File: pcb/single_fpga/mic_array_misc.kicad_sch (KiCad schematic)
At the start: 44 parts

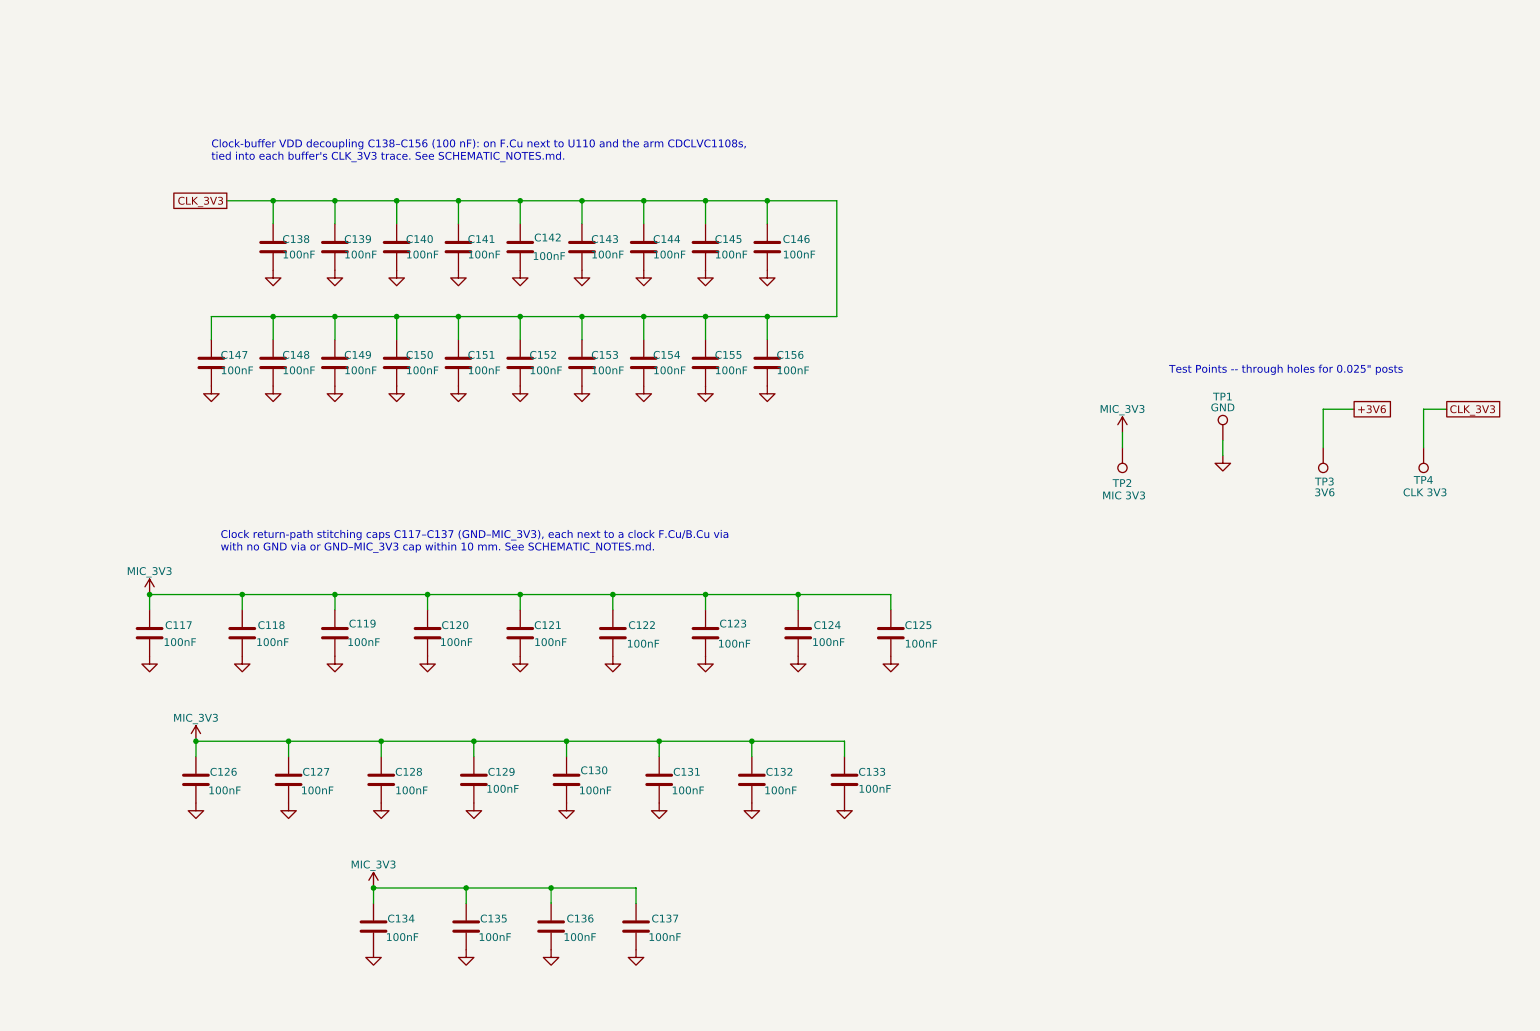
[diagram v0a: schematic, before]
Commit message: Added more stitching caps and vias. Carved +5V island in In2.Cu and renamed.
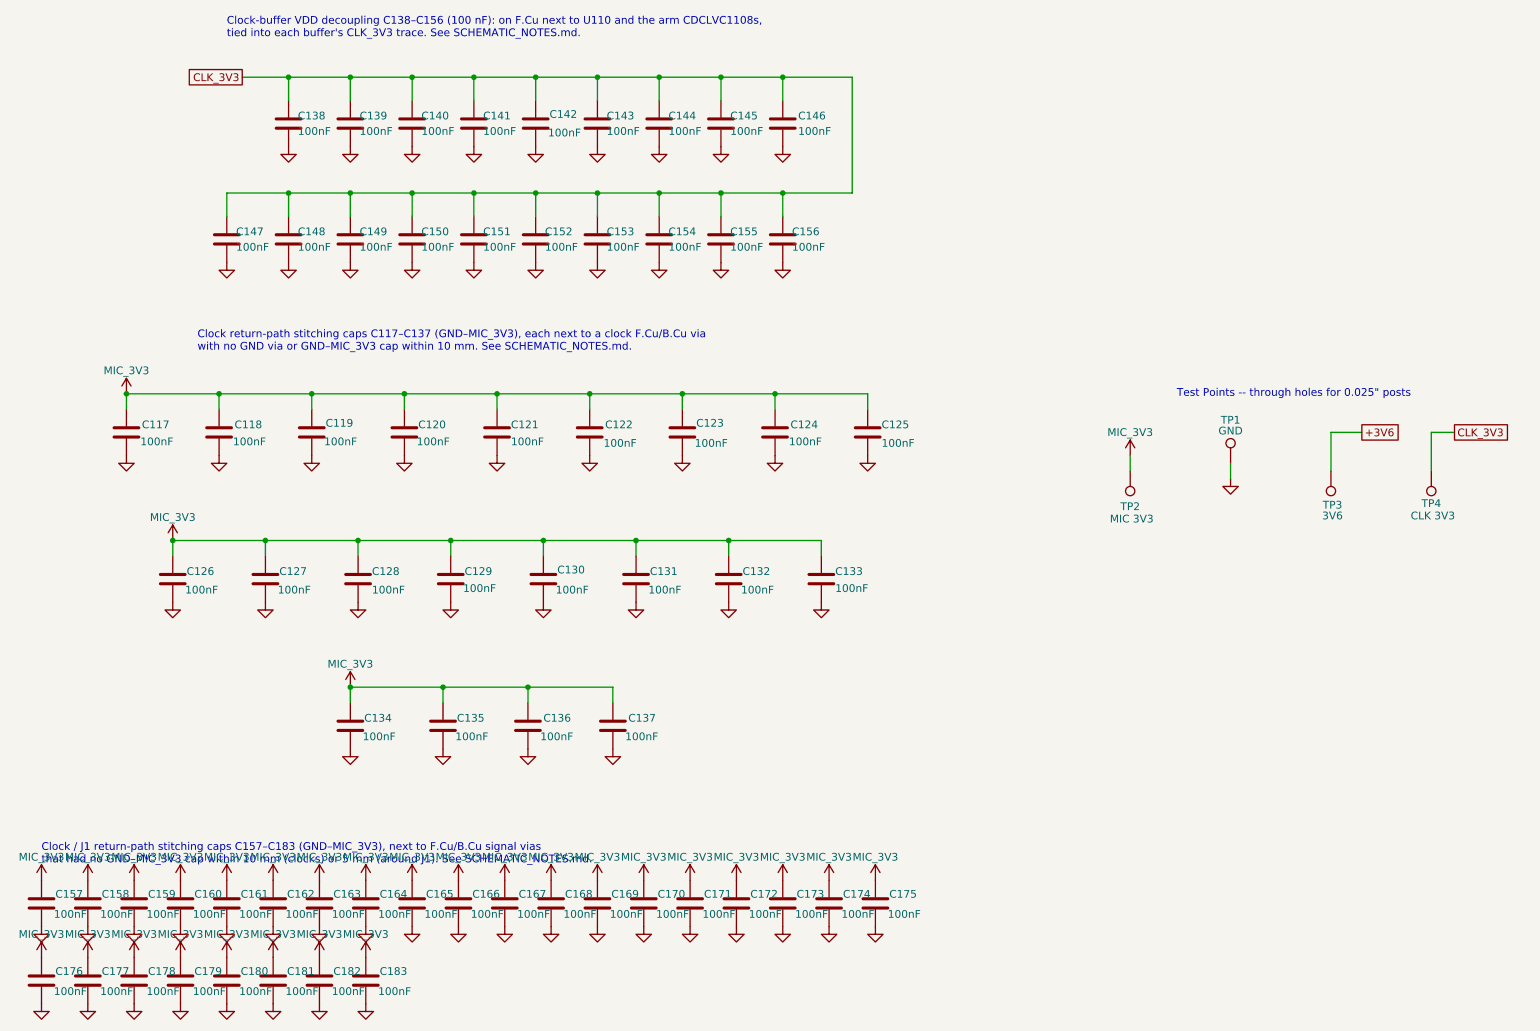
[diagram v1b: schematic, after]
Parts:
- added C157, C158, C159, C160, C161, C162, C163, C164, C165, C166, C167, C168, C169, C170, C171, C172, C173, C174, C175, C176, C177, C178, C179, C180, C181, C182, C183: 100nF, Capacitor_SMD:C_0603_1608Metric, symbol Device:C
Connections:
- net GND: now also C157.2, C158.2, C159.2, C160.2, C161.2, C162.2, C163.2, C164.2, C165.2, C166.2, C167.2, C168.2, C169.2, C170.2, C171.2, C172.2, C173.2, C174.2, C175.2, C176.2, C177.2, C178.2, C179.2, C180.2, C181.2, C182.2, C183.2
- net MIC_3V3: now also C157.1, C158.1, C159.1, C160.1, C161.1, C162.1, C163.1, C164.1, C165.1, C166.1, C167.1, C168.1, C169.1, C170.1, C171.1, C172.1, C173.1, C174.1, C175.1, C176.1, C177.1, C178.1, C179.1, C180.1, C181.1, C182.1, C183.1
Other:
- note added: "Clock / J1 return-path stitching caps C157–C183 (GND–MIC_3V3), next to F.Cu/B.Cu signal vias that had no GND–MIC_3V3 cap within 10 mm (clocks) or 5 mm (around J1). See SCHEMATIC_NOTES.md."
- moved on the sheet: C117, C118, C119, C120, C121, C122, C123, C124, C125, C126, C127, C128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
